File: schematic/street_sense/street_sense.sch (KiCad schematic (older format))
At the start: 9 parts, among them J1 USB_B_Micro, Q1 FQP27P06, U1 Lolin_D32_Pro, U2 5V_DC_DC_BOOST, U3 plantower_pms5003

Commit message: Updated Schematic
added the following components:
- Ozone sensor
- NO2 sensor
- OLED 128x64 display
- ADS1015 12-bit ADC
- DS3231 RTC
- Adafruit I2S MEMS Microphone
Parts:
- added U4: Adafruit_I2S_MEMS_Mic, symbol mike_library:Adafruit_I2S_MEMS_Mic
- added U5: I2C_OLED_128x64, symbol mike_library:I2C_OLED_128x64
- added U6: ADS1015IDGS, Package_SO:TSSOP-10_3x3mm_P0.5mm, symbol Analog_ADC:ADS1015IDGS
- added U7: DS3231M, Package_SO:SOIC-16W_7.5x10.3mm_P1.27mm, symbol Timer_RTC:DS3231M
- added U8: ULPSM-O3, symbol mike_library:ULPSM-O3
- added U9: ULPSM-NO2, symbol mike_library:ULPSM-NO2
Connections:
- net labels added: +3.3V, +5V
- wire segments 37 -> 89
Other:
- moved on the sheet: BAT1, C1, J1, Q1, R1, U1, U2, U3

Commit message: added pulldown resistor to I2S microphone
100k ohm pulldown from DOUT to GND
as described in manufacturer's datasheet
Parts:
- added R2: 100k, symbol Device:R
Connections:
- wire segments 89 -> 90
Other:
- note added: "Notes:\n- add schematic notes here"
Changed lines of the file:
@@
 Sheet 1 1
 Title "Street Sense"
-Date "2019-02-08"
-Rev "v02"
+Date "2019-02-12"
+Rev "v03"
 Comp ""
 Comment1 ""
@@
 Wire Wire Line
 	4450 4150 4500 4150
-$Comp
-L power:GND #PWR03
-U 1 1 5C5E6B7E
-P 4450 4750
-F 0 "#PWR03" H 4450 4500 50  0001 C CNN
-F 1 "GND" H 4455 4577 50  0000 C CNN
-F 2 "" H 4450 4750 50  0001 C CNN
-F 3 "" H 4450 4750 50  0001 C CNN
-	1    4450 4750
-	1    0    0    -1
-$EndComp
-Wire Wire Line
-	4450 4750 4450 4650
-Wire Wire Line
-	4450 4650 4500 4650
-Wire Wire Line
-	4500 2850 4200 2850
-Wire Wire Line
-	4200 2850 4200 4550
-Wire Wire Line
-	4200 4550 4500 4550
+Wire Wire Line
+	4500 4800 4500 4650
+Wire Wire Line
+	4500 2850 4100 2850
+Wire Wire Line
+	4100 2850 4100 4550
+Wire Wire Line
+	4100 4550 4500 4550
 Wire Wire Line
 	4500 2950 4300 2950
@@
 	4300 2950 4300 4350
 Wire Wire Line
-	4500 3050 4100 3050
-Wire Wire Line
-	4100 3050 4100 4450
-Wire Wire Line
-	4100 4450 4500 4450
+	4500 3050 4200 3050
+Wire Wire Line
+	4200 3050 4200 4450
+Wire Wire Line
+	4200 4450 4500 4450
 Wire Wire Line
 	4300 4350 4500 4350
@@
 $EndComp
 Connection ~ 3900 1400
+$Comp
+L Device:R R2
+U 1 1 5C630AD4
+P 4200 4750
+F 0 "R2" H 4270 4796 50  0000 L CNN
+F 1 "100k" H 4270 4705 50  0000 L CNN
+F 2 "" V 4130 4750 50  0001 C CNN
+F 3 "~" H 4200 4750 50  0001 C CNN
+	1    4200 4750
+	1    0    0    -1
+$EndComp
+$Comp
+L power:GND #PWR03
+U 1 1 5C5E6B7E
+P 4500 4800
+F 0 "#PWR03" H 4500 4550 50  0001 C CNN
+F 1 "GND" H 4505 4627 50  0000 C CNN
+F 2 "" H 4500 4800 50  0001 C CNN
+F 3 "" H 4500 4800 50  0001 C CNN
+	1    4500 4800
+	1    0    0    -1
+$EndComp
+$Comp
+L power:GND #PWR016
+U 1 1 5C6325CC
+P 4200 4950
+F 0 "#PWR016" H 4200 4700 50  0001 C CNN
+F 1 "GND" H 4205 4777 50  0000 C CNN
+F 2 "" H 4200 4950 50  0001 C CNN
+F 3 "" H 4200 4950 50  0001 C CNN
+	1    4200 4950
+	1    0    0    -1
+$EndComp
+Wire Wire Line
+	4200 4450 4200 4600
+Connection ~ 4200 4450
+Wire Wire Line
+	4200 4950 4200 4900
+Wire Notes Line
+	1250 6500 1250 7500
+Wire Notes Line
+	1250 7500 3650 7500
+Wire Notes Line
+	3650 7500 3650 6500
+Wire Notes Line
+	3650 6500 1250 6500
+Text Notes 1400 6750 0    50   ~ 0
+Notes:\n- add schematic notes here
 $EndSCHEMATC

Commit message: updated schematic
added components to reduce power supply rail noise
created by DC-DC boost converter
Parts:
- removed D1: 1N4001, Diode_THT:D_DO-41_SOD81_P10.16mm_Horizontal, symbol Diode:1N4001
- added C2: 220uF, symbol Device:CP1
- added D1: MBD 301, symbol Device:D_Schottky
- added Q2: PN2222A, Package_TO_SOT_THT:TO-92_Inline, symbol Transistor_BJT:PN2222A
- added Q3: FQP27P06, digikey-footprints:TO-220-3, symbol dk_Transistors-FETs-MOSFETs-Single:FQP27P06
- added R3: 1k, symbol Device:R
- added R4: 10k, symbol Device:R
- R1: value 100k -> 10k
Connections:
- net labels removed: +5V
- wire segments 90 -> 107
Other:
- moved on the sheet: BAT1, C1, J1, Q1, R1, R2, U1, U2, U3, U4, U5, U7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

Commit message: integrated ADS1219 ADC into design (code + schematic)
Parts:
- removed U6: ADS1015IDGS, Package_SO:TSSOP-10_3x3mm_P0.5mm, symbol Analog_ADC:ADS1015IDGS
- added C3: 0.1uF, symbol Device:C_Small
- added R5: 100k, symbol Device:R
- added U6: ADS1219, Package_SO:TSSOP-16_4.4x5mm_P0.65mm, symbol mike_library:ADS1219
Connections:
- wire segments 107 -> 134
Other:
- moved on the sheet: U5, U7, U8, U9

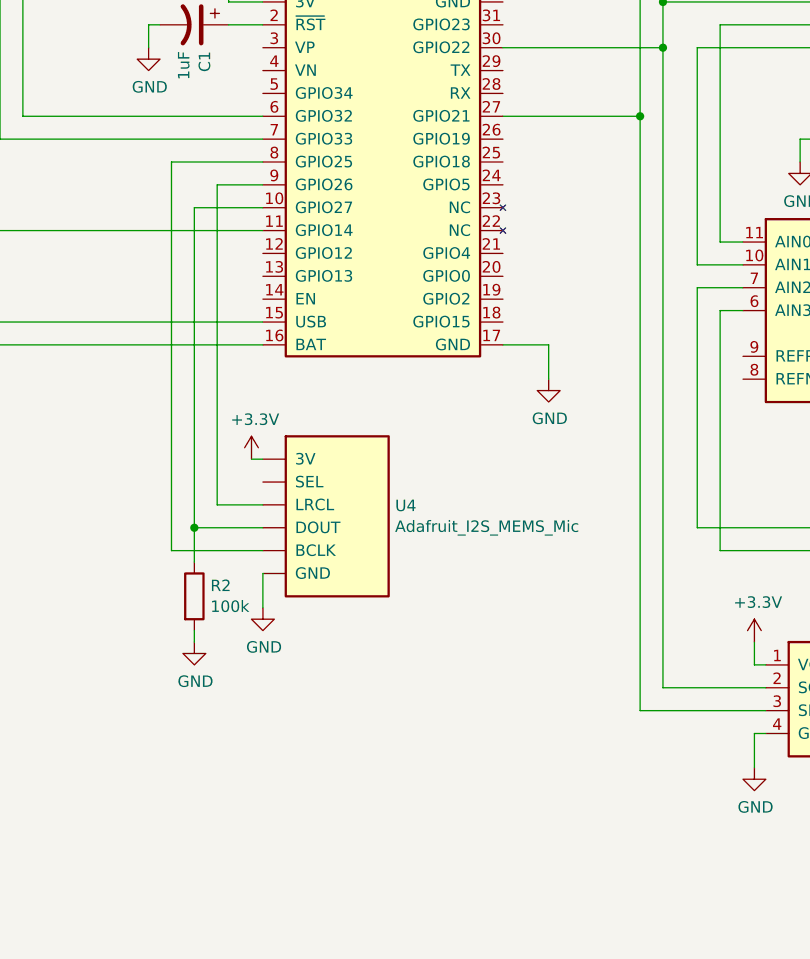
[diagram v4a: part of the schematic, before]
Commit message: updated uPy code and schematic V06 with new I2S microphone
Replaced Adafruit SPH0645LM4H I2S microphone with INMP441 I2S microphone
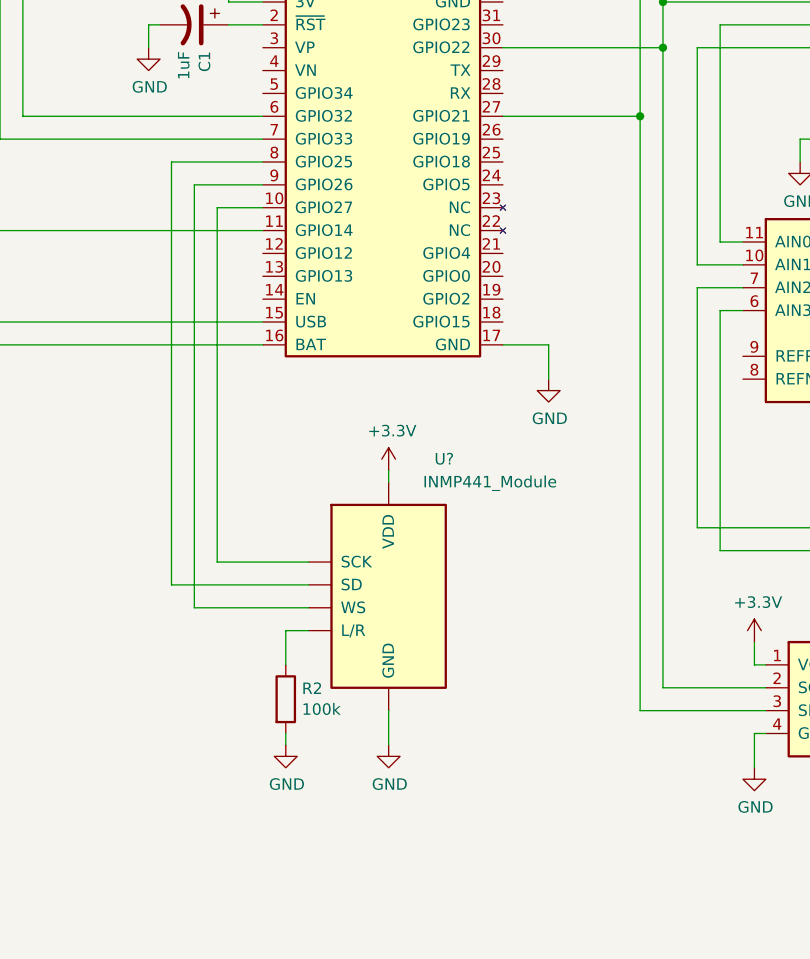
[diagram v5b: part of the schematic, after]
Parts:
- removed U4: Adafruit_I2S_MEMS_Mic, symbol mike_library:Adafruit_I2S_MEMS_Mic
- added U?: INMP441_Module, symbol mike_library:INMP441_Module
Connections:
- net +3V3: now also U?.~ (WS)
- net GND: now also U?.~ (WS)
- net at U1.10 (GPIO27): now also U?.~ (WS); no longer R2.1
- net at U1.8 (GPIO25): now also U?.~ (WS)
- net at U1.9 (GPIO26): now also U?.~ (WS)
- new net: R2.1, U?.~ (WS)
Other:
- moved on the sheet: R2
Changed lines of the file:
@@
 Sheet 1 1
 Title "Street Sense"
-Date "2019-03-17"
-Rev "v05"
+Date "2019-03-20"
+Rev "v06"
 Comp ""
 Comment1 ""
@@
 	1500 1300 1600 1300
 $Comp
-L mike_library:Adafruit_I2S_MEMS_Mic U4
-U 1 1 5C5DDDEB
-P 5800 4700
-F 0 "U4" H 6028 4296 50  0000 L CNN
-F 1 "Adafruit_I2S_MEMS_Mic" H 6028 4205 50  0000 L CNN
-F 2 "" H 5800 4700 50  0001 C CNN
-F 3 "" H 5800 4700 50  0001 C CNN
-	1    5800 4700
-	1    0    0    -1
-$EndComp
-$Comp
 L power:+3.3V #PWR01
 U 1 1 5C5DE17A
@@
 L power:+3.3V #PWR02
 U 1 1 5C5E2A6A
-P 5400 4900
-F 0 "#PWR02" H 5400 4750 50  0001 C CNN
-F 1 "+3.3V" H 5415 5073 50  0000 C CNN
-F 2 "" H 5400 4900 50  0001 C CNN
-F 3 "" H 5400 4900 50  0001 C CNN
-	1    5400 4900
-	1    0    0    -1
-$EndComp
-Wire Wire Line
-	5400 4900 5450 4900
-Wire Wire Line
-	5450 5550 5450 5400
+P 6000 4950
+F 0 "#PWR02" H 6000 4800 50  0001 C CNN
+F 1 "+3.3V" H 6015 5123 50  0000 C CNN
+F 2 "" H 6000 4950 50  0001 C CNN
+F 3 "" H 6000 4950 50  0001 C CNN
+	1    6000 4950
+	1    0    0    -1
+$EndComp
+Wire Wire Line
+	6000 6150 6000 6000
 Wire Wire Line
 	5450 3600 5050 3600
 Wire Wire Line
-	5050 3600 5050 5300
-Wire Wire Line
-	5050 5300 5450 5300
-Wire Wire Line
-	5450 3700 5250 3700
-Wire Wire Line
-	5250 3700 5250 5100
-Wire Wire Line
-	5450 3800 5150 3800
-Wire Wire Line
-	5150 3800 5150 5200
-Wire Wire Line
-	5150 5200 5450 5200
-Wire Wire Line
-	5250 5100 5450 5100
+	5450 3700 5150 3700
+Wire Wire Line
+	5450 3800 5250 3800
 Wire Wire Line
 	6500 4400 6700 4400
@@
 L Device:R R2
 U 1 1 5C630AD4
-P 5150 5500
-F 0 "R2" H 5220 5546 50  0000 L CNN
-F 1 "100k" H 5220 5455 50  0000 L CNN
-F 2 "" V 5080 5500 50  0001 C CNN
-F 3 "~" H 5150 5500 50  0001 C CNN
-	1    5150 5500
+P 5550 5950
+F 0 "R2" H 5620 5996 50  0000 L CNN
+F 1 "100k" H 5620 5905 50  0000 L CNN
+F 2 "" V 5480 5950 50  0001 C CNN
+F 3 "~" H 5550 5950 50  0001 C CNN
+	1    5550 5950
 	1    0    0    -1
 $EndComp
@@
 L power:GND #PWR03
 U 1 1 5C5E6B7E
-P 5450 5550
-F 0 "#PWR03" H 5450 5300 50  0001 C CNN
-F 1 "GND" H 5455 5377 50  0000 C CNN
-F 2 "" H 5450 5550 50  0001 C CNN
-F 3 "" H 5450 5550 50  0001 C CNN
-	1    5450 5550
+P 6000 6150
+F 0 "#PWR03" H 6000 5900 50  0001 C CNN
+F 1 "GND" H 6005 5977 50  0000 C CNN
+F 2 "" H 6000 6150 50  0001 C CNN
+F 3 "" H 6000 6150 50  0001 C CNN
+	1    6000 6150
 	1    0    0    -1
 $EndComp
@@
 L power:GND #PWR016
 U 1 1 5C6325CC
-P 5150 5700
-F 0 "#PWR016" H 5150 5450 50  0001 C CNN
-F 1 "GND" H 5155 5527 50  0000 C CNN
-F 2 "" H 5150 5700 50  0001 C CNN
-F 3 "" H 5150 5700 50  0001 C CNN
-	1    5150 5700
-	1    0    0    -1
-$EndComp
-Wire Wire Line
-	5150 5200 5150 5350
-Connection ~ 5150 5200
-Wire Wire Line
-	5150 5700 5150 5650
+P 5550 6150
+F 0 "#PWR016" H 5550 5900 50  0001 C CNN
+F 1 "GND" H 5555 5977 50  0000 C CNN
+F 2 "" H 5550 6150 50  0001 C CNN
+F 3 "" H 5550 6150 50  0001 C CNN
+	1    5550 6150
+	1    0    0    -1
+$EndComp
+Wire Wire Line
+	5550 5650 5550 5800
+Wire Wire Line
+	5550 6150 5550 6100
 Wire Notes Line
 	1250 6500 1250 7500
@@
 Wire Wire Line
 	8250 3650 8250 3750
+$Comp
+L mike_library:INMP441_Module U?
+U 1 1 5C92A64F
+P 6000 5000
+F 0 "U?" H 6200 5100 50  0000 L CNN
+F 1 "INMP441_Module" H 6150 5000 50  0000 L CNN
+F 2 "" H 6000 5000 50  0001 C CNN
+F 3 "" H 6000 5000 50  0001 C CNN
+	1    6000 5000
+	1    0    0    -1
+$EndComp
+Wire Wire Line
+	5550 5650 5650 5650
+Wire Wire Line
+	5250 5350 5650 5350
+Wire Wire Line
+	5050 3600 5050 5450
+Wire Wire Line
+	5250 3800 5250 5350
+Wire Wire Line
+	5150 5550 5650 5550
+Wire Wire Line
+	5150 3700 5150 5550
+Wire Wire Line
+	5050 5450 5650 5450
+Wire Wire Line
+	6000 4950 6000 5000
 $EndSCHEMATC
